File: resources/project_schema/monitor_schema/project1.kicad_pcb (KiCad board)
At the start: 2 copper layers, 24 parts, among them J1 Conn_01x02, J2 Conn_01x03, J3 Conn_01x04, J4 Conn_01x06, J5 Conn_01x03, J6 Conn_01x03, Q1 BSS138, Q2 BSS84, SW1 SW_MEC_5E, SW2 SW_MEC_5E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

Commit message: Update pcb layout
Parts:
- moved J4 50.3 mm to (163.6, 108.7), turned to 180 degrees
- moved J3 45.4 mm to (163.6, 89.9), turned to 180 degrees
- moved J2 35.6 mm to (163.1, 120.9), turned to 180 degrees
- moved U1 21.6 mm to (104.6, 87.4)
- moved C1 21.6 mm to (96.0, 86.9)
- moved C2 21.6 mm to (104.7, 80.3)
- moved J1 21.6 mm to (87.9, 85.9)
- moved R2 20.0 mm to (129.0, 117.9)
- moved D1 15.5 mm to (107.4, 100.3)
- moved D2 15.5 mm to (107.4, 104.1)
- moved Q2 15.5 mm to (104.9, 110.5)
- moved R5 15.5 mm to (109.2, 109.7)
- moved R6 15.5 mm to (104.9, 115.6)
- moved R7 15.5 mm to (104.7, 119.4)
- moved Q1 15.5 mm to (113.5, 110.2)
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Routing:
- net /Vin: track 0.00 -> 194.3 mm
- net /esp32/BATT_V: track 0.00 -> 38.9 mm
- net /esp32/CS: track 0.00 -> 31.6 mm
- net /esp32/CLK: track 0.00 -> 30.1 mm
- net /esp32/MISO: track 0.00 -> 28.5 mm
- net /esp32/BOOT: track 0.00 -> 26.2 mm
- net /esp32/TX: track 0.00 -> 24.4 mm
- net /esp32/WIFI_CONNECTION: track 0.00 -> 24.4 mm
- net /esp32/RX: track 0.00 -> 23.9 mm
- net /esp32/NO_WIFI_CONNECTION: track 0.00 -> 21.7 mm
- net /Vbat: track 0.00 -> 15.4 mm
- net Net-(C3-Pad2): track 0.00 -> 10.9 mm
- net Net-(Q1-Pad3): track 0.00 -> 7.15 mm
- net /esp32/EN: track 0.00 -> 5.30 mm
- net Net-(Q2-Pad3): track 0.00 -> 5.08 mm
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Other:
- board outline added: 78.7 x 56.4 mm
- net class info added: clearance 0.3, trace_width 0.6, via_dia 0.7, via_drill 0.5
- net class power added: clearance 0.3, trace_width 1, via_dia 1.1, via_drill 0.5

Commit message: Pequeña modificación del esquematico
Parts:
- moved R2 37.1 mm to (116.0, 83.1), turned to 270 degrees
- moved D2 31.1 mm to (113.7, 73.7)
- moved R3 30.9 mm to (119.5, 73.9)
- moved SW1 27.4 mm to (115.3, 90.9), turned to 90 degrees
- moved J6 27.0 mm to (90.0, 85.8)
- moved D1 24.2 mm to (113.7, 77.0)
- moved R1 24.2 mm to (119.8, 77.0)
- moved C3 19.2 mm to (115.4, 98.3), turned to 180 degrees
- moved C1 12.9 mm to (95.9, 73.9)
- moved J1 12.8 mm to (91.1, 73.5)
- moved U1 8.80 mm to (102.2, 78.9)
- moved C2 7.53 mm to (108.8, 73.9), turned to 90 degrees
- moved J5 5.19 mm to (90.0, 94.6)
- moved J2 2.45 mm to (160.9, 119.7)
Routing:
- net /GND: track 0.00 -> 166.4 mm
- net /esp32/GNRL_PURPOSE_2: track 0.00 -> 36.7 mm
- net /esp32/DATA_OUT_DTH22_SENSOR: track 0.00 -> 34.9 mm
- net /esp32/GNRL_PURPOSE_1: track 0.00 -> 33.9 mm
- net /esp32/WIFI_CONNECTION: track 24.4 -> 13.2 mm
- net /esp32/EN: track 5.30 -> 12.5 mm
- net /Vin: track 194.3 -> 198.1 mm
- net Net-(C3-Pad2): track 10.9 -> 8.07 mm
- net /Vbat: track 15.4 -> 13.4 mm
- net /esp32/NO_WIFI_CONNECTION: track 21.7 -> 20.1 mm

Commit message: Adelanto de PCB
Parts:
- moved J3 26.3 mm to (144.3, 107.7)
- moved R7 25.1 mm to (105.3, 94.3), turned to -90 degrees
- moved R5 22.9 mm to (100.3, 88.7), turned to 0 degrees
- moved R6 22.8 mm to (100.3, 93.3)
- moved C1 22.6 mm to (96.1, 96.6)
- moved D1 22.6 mm to (113.9, 99.6)
- moved J5 22.6 mm to (90.2, 117.3)
- moved J6 22.6 mm to (90.2, 108.4)
- moved R1 22.6 mm to (119.9, 99.6)
- moved SW1 22.6 mm to (115.5, 113.5)
- moved C2 22.6 mm to (108.9, 96.6)
- moved C3 22.6 mm to (115.5, 121.0)
- moved D2 22.6 mm to (113.9, 96.4)
- moved J1 22.6 mm to (91.3, 96.1)
- moved R2 22.6 mm to (116.2, 105.8)
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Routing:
- net /Vin: track 198.1 -> 119.1 mm
- net /esp32/READ_BATT_V: track 0.00 -> 49.7 mm
- net /GND: track 166.4 -> 133.6 mm
- net /esp32/MOSI: track 0.00 -> 25.6 mm
- net /esp32/DATA_OUT_DTH22_SENSOR: track 34.9 -> 13.9 mm
- net /esp32/TX: track 24.4 -> 4.16 mm
- net /esp32/RX: track 23.9 -> 5.00 mm
- net /esp32/BOOT: track 26.2 -> 8.54 mm
- net /esp32/BATT_V: track 38.9 -> 48.2 mm
- net /esp32/MISO: track 28.5 -> 19.9 mm
- net /esp32/CLK: track 30.1 -> 24.4 mm
- net Net-(Q1-Pad3): track 7.15 -> 12.7 mm
- net /esp32/CS: track 31.6 -> 27.2 mm
- net Net-(Q2-Pad3): track 5.08 -> 3.79 mm
- net /esp32/NO_WIFI_CONNECTION: track 20.1 -> 19.1 mm
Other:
- board size 78.7 x 56.4 mm -> 79 x 56.4 mm
- net class Default removed
- net class info removed
- net class power removed

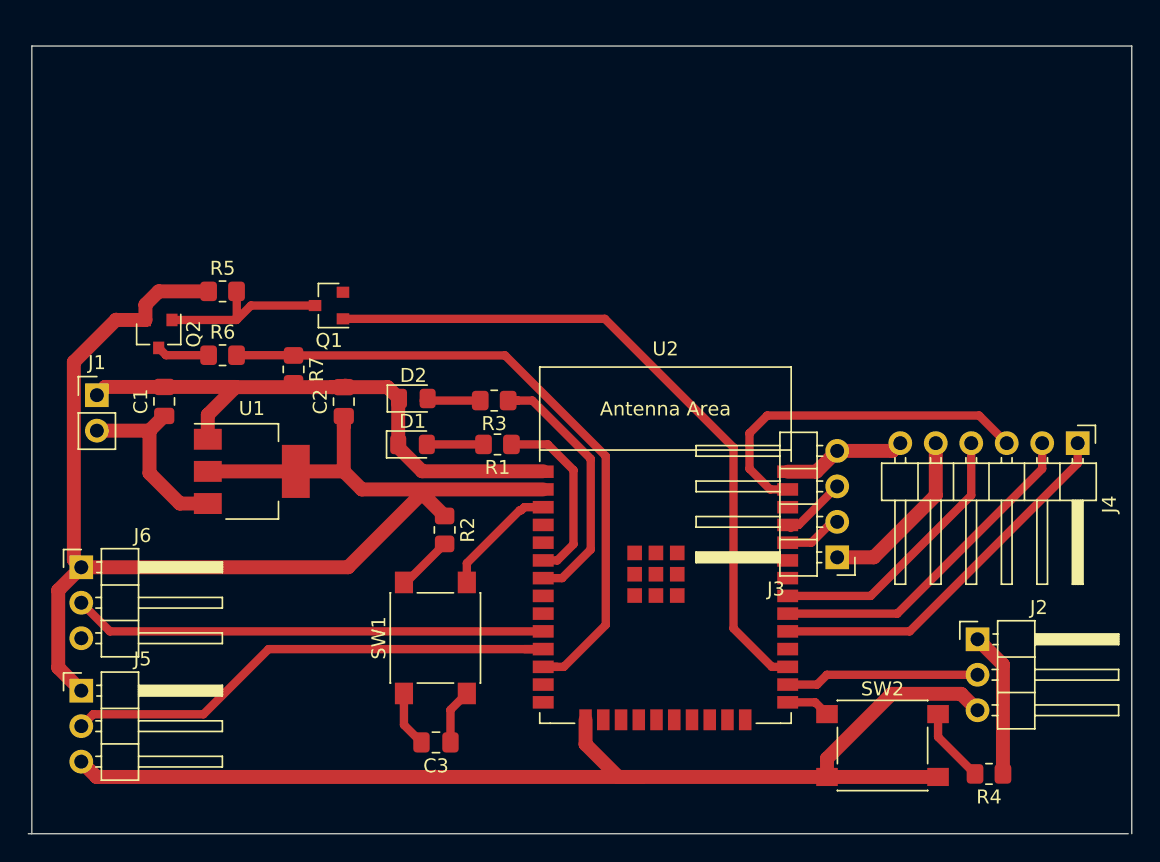
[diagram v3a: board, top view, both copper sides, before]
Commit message: Modificación PCB por dos caras
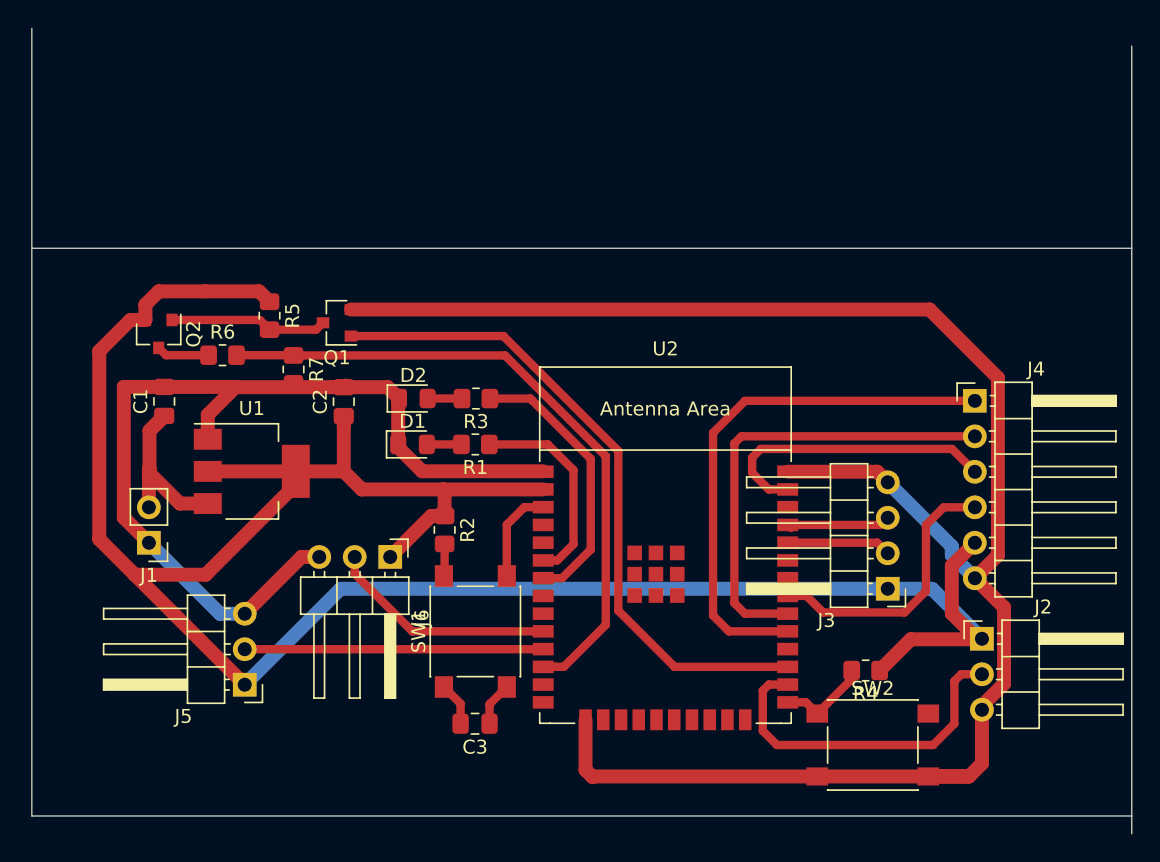
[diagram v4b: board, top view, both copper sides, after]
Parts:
- moved J6 22.1 mm to (112.3, 107.7), turned to -90 degrees
- moved J5 11.7 mm to (101.9, 116.8), turned to 180 degrees
- moved R4 11.5 mm to (146.3, 115.8)
- moved J1 11.2 mm to (95.0, 106.7), turned to 180 degrees
- moved J4 7.96 mm to (154.1, 96.5), turned to 0 degrees
- moved J3 4.26 mm to (147.9, 110.0)
- moved R5 3.79 mm to (103.6, 90.4), turned to -90 degrees
- moved C3 3.10 mm to (118.3, 119.6)
- moved SW1 2.90 mm to (118.4, 113.0)
- moved R1 1.58 mm to (118.4, 99.6)
- moved Q1 1.36 mm to (108.5, 90.9)
- moved R3 1.31 mm to (118.4, 96.4)
- moved SW2 0.70 mm to (146.8, 121.2)
- moved J2 0.32 mm to (154.6, 113.6)
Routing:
- net /GND: track 133.6 -> 198.2 mm
- net /Vin: track 119.1 -> 167.2 mm
- net /esp32/GNRL_PURPOSE_1: track 33.9 -> 16.4 mm
- net /esp32/GNRL_PURPOSE_2: track 36.7 -> 21.4 mm
- net /esp32/CS: track 27.2 -> 38.6 mm
- net /esp32/DATA_OUT_DTH22_SENSOR: track 13.9 -> 24.8 mm
- net /esp32/CLK: track 24.4 -> 33.0 mm
- net /esp32/MOSI: track 25.6 -> 21.0 mm
- net /esp32/TX: track 4.16 -> 7.48 mm
- net /esp32/RX: track 5.00 -> 7.69 mm
- net Net-(C3-Pad2): track 8.07 -> 5.44 mm
- net /esp32/EN: track 12.5 -> 9.93 mm
- net /esp32/BOOT: track 8.54 -> 6.56 mm
- net /esp32/READ_BATT_V: track 49.7 -> 47.8 mm
- net Net-(D2-Pad2): track 4.06 -> 2.46 mm
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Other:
- board size 79 x 56.4 mm -> 78.7 x 57.7 mm

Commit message: Update pcb layout
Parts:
- J2: footprint Connector_PinHeader_2.54mm:PinHeader_1x03_P2.54mm_Horizontal -> Connector_PinHeader_2.54mm:PinHeader_1x04_P2.54mm_Vertical
- J3: footprint Connector_PinHeader_2.54mm:PinHeader_1x04_P2.54mm_Horizontal -> Connector_PinHeader_2.54mm:PinHeader_1x04_P2.54mm_Vertical
- J4: footprint Connector_PinHeader_2.54mm:PinHeader_1x06_P2.54mm_Horizontal -> Connector_PinHeader_2.54mm:PinHeader_1x06_P2.54mm_Vertical
- J5, J6: footprint Connector_PinHeader_2.54mm:PinHeader_1x03_P2.54mm_Horizontal -> Connector_PinHeader_2.54mm:PinHeader_1x03_P2.54mm_Vertical
- moved R5 74.1 mm to (88.9, 163.1), turned to 0 degrees
- moved D2 73.1 mm to (84.1, 163.1)
- moved Q1 61.6 mm to (107.3, 152.5), turned to 0 degrees
- moved Q2 59.5 mm to (93.4, 151.2), turned to 0 degrees
- moved SW1 58.0 mm to (73.2, 149.4), turned to 180 degrees
- moved R7 57.5 mm to (102.7, 151.7), turned to 0 degrees
- moved R6 56.0 mm to (107.4, 148.8)
- moved J2 50.7 mm to (128.5, 157.0), turned to 270 degrees
- moved R3 48.6 mm to (109.1, 144.0), turned to 0 degrees
- moved D1 47.5 mm to (102.7, 145.8)
- moved C3 46.0 mm to (83.3, 149.4), turned to 270 degrees
- moved R1 39.6 mm to (109.1, 138.1), turned to 0 degrees
- moved J1 38.1 mm to (56.9, 108.2), turned to 0 degrees
- moved J4 37.6 mm to (145.3, 133.1), turned to 180 degrees
- moved R2 36.0 mm to (109.1, 141.1), turned to 0 degrees
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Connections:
- J2 pad 3: /GND -> /esp32/CLK_SENSOR
- U2 pad 14: Net-(U2-Pad14) -> /esp32/READ_BATT_V
- U2 pad 23: Net-(U2-Pad23) -> /esp32/CLK_SENSOR
- U2 pad 24: Net-(U2-Pad24) -> /esp32/DATA_OUT_DTH22_SENSOR
- U2 pad 26: /esp32/DATA_OUT_DTH22_SENSOR -> Net-(U2-Pad26)
- U2 pad 27: /esp32/READ_BATT_V -> Net-(U2-Pad27)
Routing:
- net /GND: track 198.2 -> 0.00 mm
- net /Vin: track 167.2 -> 0.00 mm
- net /esp32/BATT_V: track 48.2 -> 0.00 mm
- net /esp32/READ_BATT_V: track 47.8 -> 0.00 mm
- net /esp32/CS: track 38.6 -> 0.00 mm
- net /esp32/CLK: track 33.0 -> 0.00 mm
- net /esp32/DATA_OUT_DTH22_SENSOR: track 24.8 -> 0.00 mm
- net /esp32/GNRL_PURPOSE_2: track 21.4 -> 0.00 mm
- net /esp32/MOSI: track 21.0 -> 0.00 mm
- net /esp32/MISO: track 19.8 -> 0.00 mm
- net /esp32/NO_WIFI_CONNECTION: track 19.7 -> 0.00 mm
- net /esp32/GNRL_PURPOSE_1: track 16.4 -> 0.00 mm
- net /esp32/WIFI_CONNECTION: track 14.7 -> 0.00 mm
- net /Vbat: track 13.7 -> 0.00 mm
- net Net-(Q1-Pad3): track 11.3 -> 0.00 mm
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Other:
- board outline removed
- net class Default added: clearance 0.2, trace_width 0.25, via_dia 0.8, via_drill 0.4
- net class info added: clearance 0.3, trace_width 0.6, via_dia 0.7, via_drill 0.5
- net class power added: clearance 0.3, trace_width 1, via_dia 1.1, via_drill 0.5
